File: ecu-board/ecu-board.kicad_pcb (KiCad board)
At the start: 2 copper layers, 180 x 127.5 mm, 53 parts, among them J1 MicroSquirt_connector, J10 Injector connector, J11 Cockpit connector, J12 EGO connector, J13 Chrankshaft Hall connector, J14 Camshaft Hall connector, J15 Ignition 1 connector, J16 Ignition 2 connector, J17 Camera connector, J18 Wheel Hall connector, J19 Speed sensor connector, J2 Battery power conenctor, J20 CAN connector, J3 MS_breakout_conn, J4 Motor connector, J5 Serial DB9 connector, J6 Controller connector, J7 Backlight connector, J8 IAT connector, J9 CLT connector, K1 Main power relay, K2 Start motor relay, U1 MAP Sensor

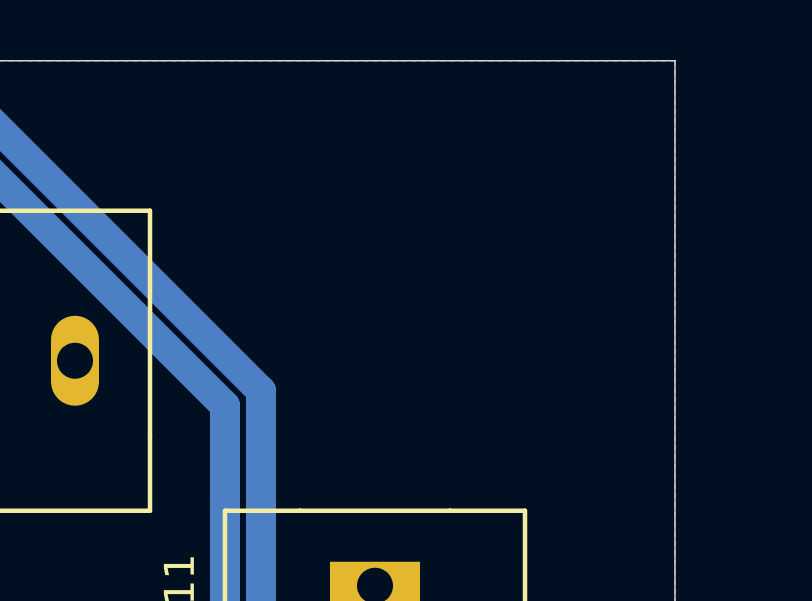
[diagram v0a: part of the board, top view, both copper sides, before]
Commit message: Create isolated M4 footprint.
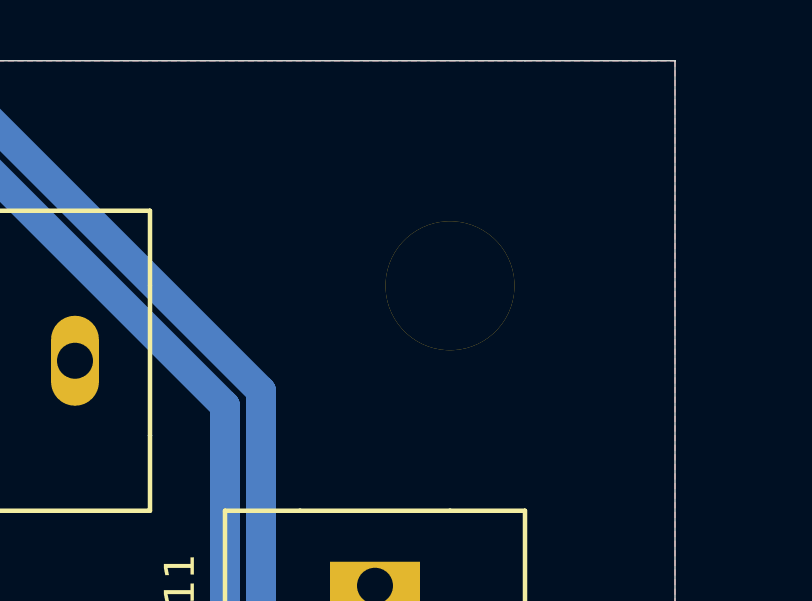
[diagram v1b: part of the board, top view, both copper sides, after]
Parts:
- added REF**: MountingHole_4.3mm_M4_DIN965_Pad_Isolated, ecu-board-footprints:MountingHole_4.3mm_M4_DIN965_Pad_Isolated, F.Cu at (222.5, 42.5)
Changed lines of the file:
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@@
     (tracks 441)
     (zones 0)
-    (modules 53)
+    (modules 54)
     (nets 63)
   )
@@
     (add_net GNDPWR)
   )
+  (module ecu-board-footprints:MountingHole_4.3mm_M4_DIN965_Pad_Isolated (layer F.Cu)
+    (at 222.5 42.5)
+    (descr "Mounting Hole 4.3mm, M4, DIN965")
+    (tags "mounting hole 4.3mm m4 din965")
+    (attr virtual)
+    (fp_text reference REF** (at 0 -4.75) (layer F.SilkS) hide
+      (effects (font (size 1 1) (thickness 0.15)))
+    )
+    (fp_text value MountingHole_4.3mm_M4_DIN965_Pad_Isolated (at 0 4.75) (layer F.Fab) hide
+      (effects (font (size 1 1) (thickness 0.15)))
+    )
+    (fp_circle (center 0 0) (end 4 0) (layer F.CrtYd) (width 0.05))
+    (fp_circle (center 0 0) (end 3.75 0) (layer Cmts.User) (width 0.15))
+    (fp_text user %R (at 0.3 0) (layer F.Fab) hide
+      (effects (font (size 1 1) (thickness 0.15)))
+    )
+    (pad 1 thru_hole circle (at 0 0) (size 4.3 4.3) (drill 4.3) (layers *.Cu *.Mask)
+      (solder_mask_margin 3.65) (solder_paste_margin 3.65) (clearance 3.8))
+  )
   (module ecu-board-footprints:TE_5747844-4 (layer F.Cu)
     (at 217.5 120 270)
@@
   (segment (start 57 40.5) (end 84 40.5) (width 2) (layer F.Cu) (net 1))
   (segment (start 55 74) (end 55 42.5) (width 2) (layer F.Cu) (net 1))
-  (segment (start 66 149.6) (end 68.499999 152.099999) (width 5) (layer B.Cu) (net 2) (status 10))
-  (segment (start 94.5 147) (end 96 148.5) (width 5) (layer B.Cu) (net 2) (status 20))
-  (segment (start 78.5 147) (end 94.5 147) (width 5) (layer B.Cu) (net 2))
-  (segment (start 69.9 149.6) (end 72.5 147) (width 5) (layer B.Cu) (net 2))
-  (segment (start 72.5 147) (end 78.5 147) (width 5) (layer B.Cu) (net 2))
-  (segment (start 94.5 152) (end 97 149.5) (width 5) (layer B.Cu) (net 2) (status 20))
-  (segment (start 68.499999 152.099999) (end 69.900001 152.099999) (width 5) (layer B.Cu) (net 2))
-  (segment (start 97 149.5) (end 75 149.5) (width 5) (layer B.Cu) (net 2) (status 30))
-  (segment (start 66 149.6) (end 69.9 149.6) (width 5) (layer B.Cu) (net 2) (status 10))
-  (segment (start 70 152) (end 94.5 152) (width 5) (layer B.Cu) (net 2))
-  (segment (start 69.900001 152.099999) (end 70 152) (width 5) (layer F.Cu) (net 2))
-  (segment (start 66 149.6) (end 68.499999 152.099999) (width 5) (layer F.Cu) (net 2) (status 10))
-  (segment (start 94.5 152) (end 97 149.5) (width 5) (layer F.Cu) (net 2) (status 20))
-  (segment (start 70 152) (end 94.5 152) (width 5) (layer F.Cu) (net 2))
-  (segment (start 68.499999 152.099999) (end 69.900001 152.099999) (width 5) (layer F.Cu) (net 2))
-  (segment (start 96 148.5) (end 96 150.5) (width 5) (layer F.Cu) (net 2) (status 30))
-  (segment (start 94.5 147) (end 96 148.5) (width 5) (layer F.Cu) (net 2) (status 20))
-  (segment (start 69.9 149.6) (end 72.5 147) (width 5) (layer F.Cu) (net 2))
-  (segment (start 66 149.6) (end 69.9 149.6) (width 5) (layer F.Cu) (net 2) (status 10))
-  (segment (start 75 149.5) (end 72.5 147) (width 5) (layer F.Cu) (net 2) (status 10))
-  (segment (start 97 149.5) (end 75 149.5) (width 5) (layer F.Cu) (net 2) (status 30))
-  (segment (start 79 146.5) (end 78.5 147) (width 0.5) (layer F.Cu) (net 2))
-  (segment (start 79 142.5) (end 79 146.5) (width 0.5) (layer F.Cu) (net 2) (status 10))
-  (segment (start 72.5 147) (end 78.5 147) (width 5) (layer F.Cu) (net 2))
-  (segment (start 78.5 147) (end 94.5 147) (width 5) (layer F.Cu) (net 2))
   (segment (start 99.84 106.34) (end 104.3 110.8) (width 1) (layer F.Cu) (net 1) (status 20))
   (segment (start 75 128.5) (end 75 125.66) (width 2) (layer F.Cu) (net 1) (status 20))
@@
   (segment (start 133.404178 102.5) (end 140.87868 102.5) (width 2) (layer F.Cu) (net 1))
   (segment (start 99.84 104) (end 99.84 106.34) (width 1) (layer F.Cu) (net 1) (status 10))
+  (segment (start 66 149.6) (end 68.499999 152.099999) (width 5) (layer B.Cu) (net 2) (status 10))
+  (segment (start 94.5 147) (end 96 148.5) (width 5) (layer B.Cu) (net 2) (status 20))
+  (segment (start 78.5 147) (end 94.5 147) (width 5) (layer B.Cu) (net 2))
+  (segment (start 69.9 149.6) (end 72.5 147) (width 5) (layer B.Cu) (net 2))
+  (segment (start 72.5 147) (end 78.5 147) (width 5) (layer B.Cu) (net 2))
+  (segment (start 94.5 152) (end 97 149.5) (width 5) (layer B.Cu) (net 2) (status 20))
+  (segment (start 68.499999 152.099999) (end 69.900001 152.099999) (width 5) (layer B.Cu) (net 2))
+  (segment (start 97 149.5) (end 75 149.5) (width 5) (layer B.Cu) (net 2) (status 30))
+  (segment (start 66 149.6) (end 69.9 149.6) (width 5) (layer B.Cu) (net 2) (status 10))
+  (segment (start 70 152) (end 94.5 152) (width 5) (layer B.Cu) (net 2))
+  (segment (start 69.900001 152.099999) (end 70 152) (width 5) (layer F.Cu) (net 2))
+  (segment (start 66 149.6) (end 68.499999 152.099999) (width 5) (layer F.Cu) (net 2) (status 10))
+  (segment (start 94.5 152) (end 97 149.5) (width 5) (layer F.Cu) (net 2) (status 20))
+  (segment (start 70 152) (end 94.5 152) (width 5) (layer F.Cu) (net 2))
+  (segment (start 68.499999 152.099999) (end 69.900001 152.099999) (width 5) (layer F.Cu) (net 2))
+  (segment (start 96 148.5) (end 96 150.5) (width 5) (layer F.Cu) (net 2) (status 30))
+  (segment (start 94.5 147) (end 96 148.5) (width 5) (layer F.Cu) (net 2) (status 20))
+  (segment (start 69.9 149.6) (end 72.5 147) (width 5) (layer F.Cu) (net 2))
+  (segment (start 66 149.6) (end 69.9 149.6) (width 5) (layer F.Cu) (net 2) (status 10))
+  (segment (start 75 149.5) (end 72.5 147) (width 5) (layer F.Cu) (net 2) (status 10))
+  (segment (start 97 149.5) (end 75 149.5) (width 5) (layer F.Cu) (net 2) (status 30))
+  (segment (start 79 146.5) (end 78.5 147) (width 0.5) (layer F.Cu) (net 2))
+  (segment (start 79 142.5) (end 79 146.5) (width 0.5) (layer F.Cu) (net 2) (status 10))
+  (segment (start 72.5 147) (end 78.5 147) (width 5) (layer F.Cu) (net 2))
+  (segment (start 78.5 147) (end 94.5 147) (width 5) (layer F.Cu) (net 2))
   (segment (start 194 150) (end 194 152.5) (width 2) (layer F.Cu) (net 2) (status 30))
   (segment (start 194 152.5) (end 197.5 152.5) (width 2) (layer F.Cu) (net 2) (status 30))

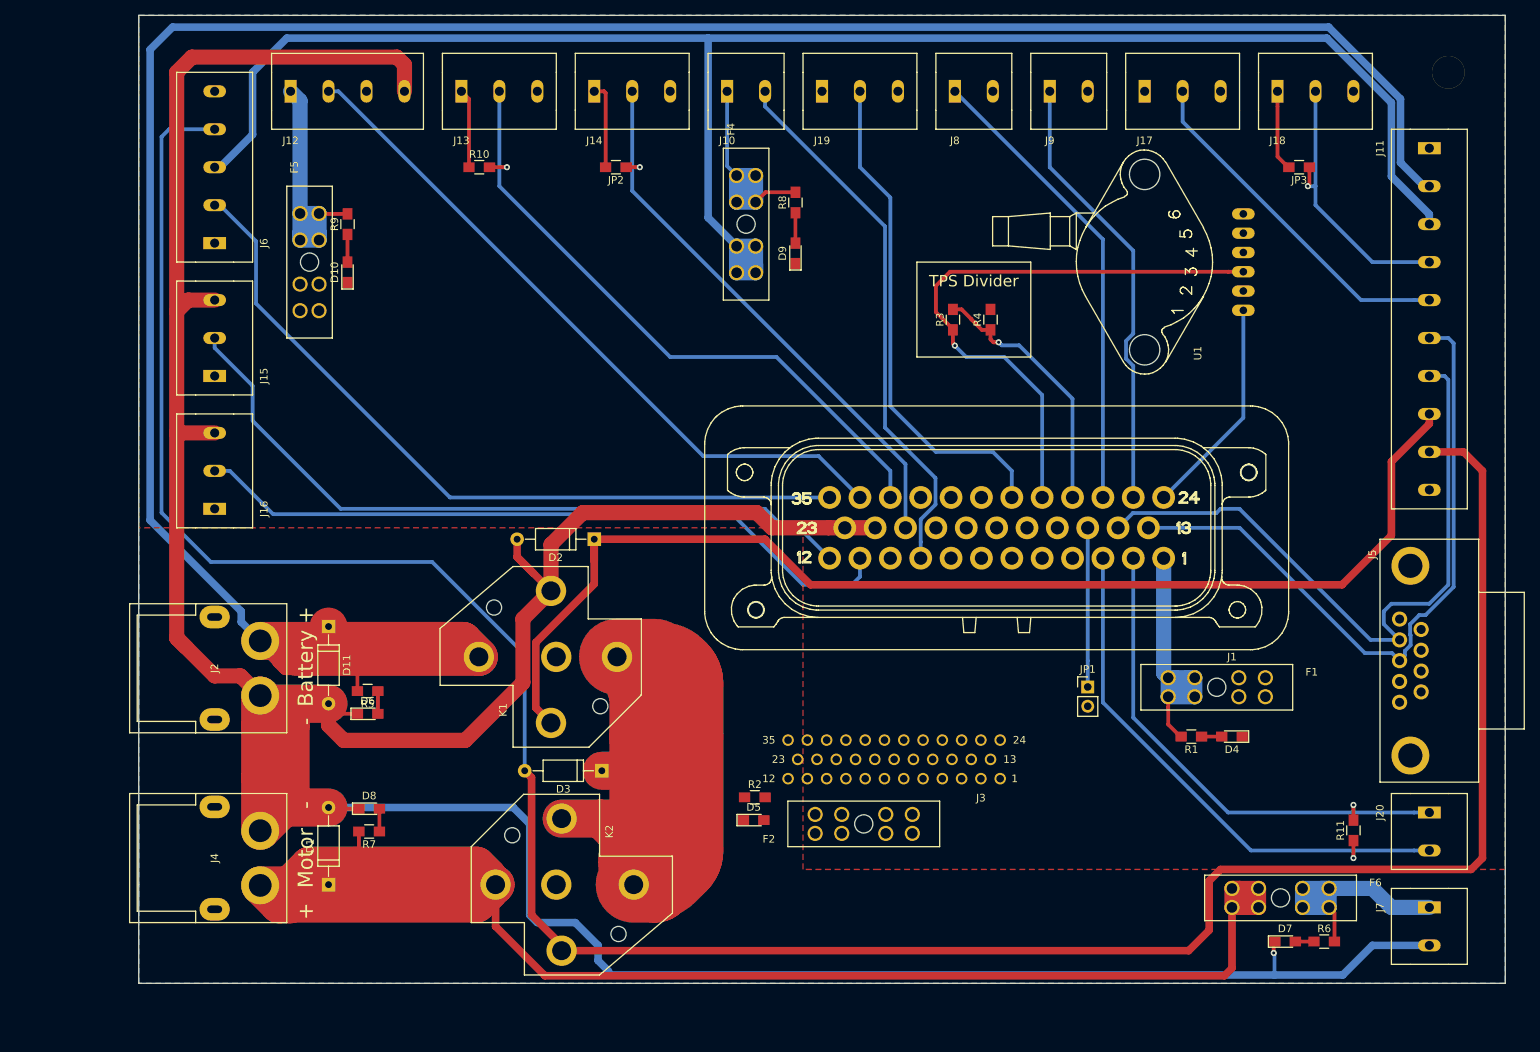
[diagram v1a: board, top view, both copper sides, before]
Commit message: Place mounting holes.
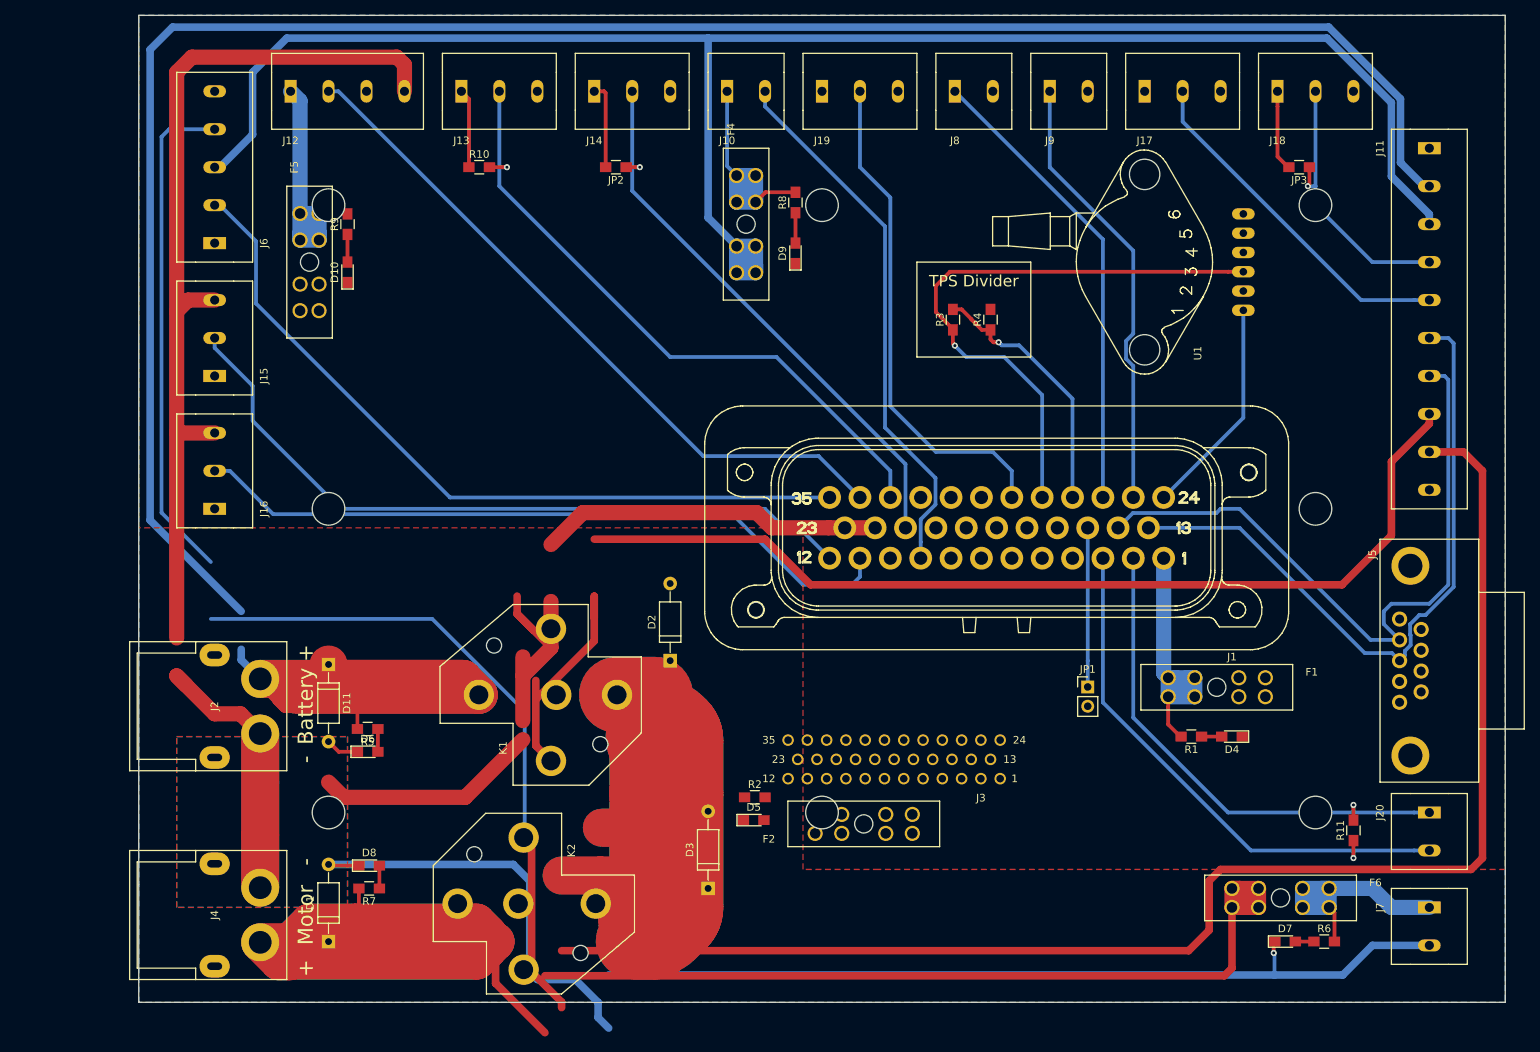
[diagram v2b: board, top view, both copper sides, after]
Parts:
- removed the REF** at (222.5, 42.5)
- added REF**: MountingHole_4.3mm_M4_DIN965_Pad_Isolated, ecu-board-footprints:MountingHole_4.3mm_M4_DIN965_Pad_Isolated, F.Cu at (75.0, 100.0)
- added REF**: MountingHole_4.3mm_M4_DIN965_Pad_Isolated, ecu-board-footprints:MountingHole_4.3mm_M4_DIN965_Pad_Isolated, F.Cu at (75.0, 140.0)
- added REF**: MountingHole_4.3mm_M4_DIN965_Pad_Isolated, ecu-board-footprints:MountingHole_4.3mm_M4_DIN965_Pad_Isolated, F.Cu at (140.0, 140.0)
- added REF**: MountingHole_4.3mm_M4_DIN965_Pad_Isolated, ecu-board-footprints:MountingHole_4.3mm_M4_DIN965_Pad_Isolated, F.Cu at (205.0, 140.0)
- added REF**: MountingHole_4.3mm_M4_DIN965_Pad_Isolated, ecu-board-footprints:MountingHole_4.3mm_M4_DIN965_Pad_Isolated, F.Cu at (205.0, 100.0)
- added REF**: MountingHole_4.3mm_M4_DIN965_Pad_Isolated, ecu-board-footprints:MountingHole_4.3mm_M4_DIN965_Pad_Isolated, F.Cu at (205.0, 60.0)
- added REF**: MountingHole_4.3mm_M4_DIN965_Pad_Isolated, ecu-board-footprints:MountingHole_4.3mm_M4_DIN965_Pad_Isolated, F.Cu at (140.0, 60.0)
- added REF**: MountingHole_4.3mm_M4_DIN965_Pad_Isolated, ecu-board-footprints:MountingHole_4.3mm_M4_DIN965_Pad_Isolated, F.Cu at (75.0, 60.0)
- moved D3 20.9 mm to (125.0, 150.0), turned to 90 degrees
- moved D2 18.9 mm to (120.0, 120.0), turned to 90 degrees
- moved D1 7.50 mm to (75.0, 157.0)
- moved D8 7.50 mm to (80.3, 147.0)
- moved J4 7.50 mm to (60.0, 153.5)
- moved R7 7.50 mm to (80.3, 150.0)
- moved K2 5.59 mm to (100.0, 152.0)
- moved D11 5.00 mm to (75.0, 120.5)
- moved D6 5.00 mm to (80.2, 132.0)
- moved J2 5.00 mm to (60.0, 126.0)
- moved K1 5.00 mm to (105.0, 124.5)
- moved R5 5.00 mm to (80.2, 129.0)
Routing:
- net GNDPWR: track 538.2 -> 459.3 mm
- added copper zone on B.Cu, net GNDPWR
- added copper zone on F.Cu, net GNDPWR
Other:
- board size 180 x 127.5 mm -> 180 x 130 mm
